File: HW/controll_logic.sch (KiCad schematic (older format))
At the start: 24 parts, among them J5 POWER_IN, J6 JTAG, J8 Stop System, SW1 RESET, U10 TL7705B, U11 ispMACH4A, U9 74HC74, X2 16MHz

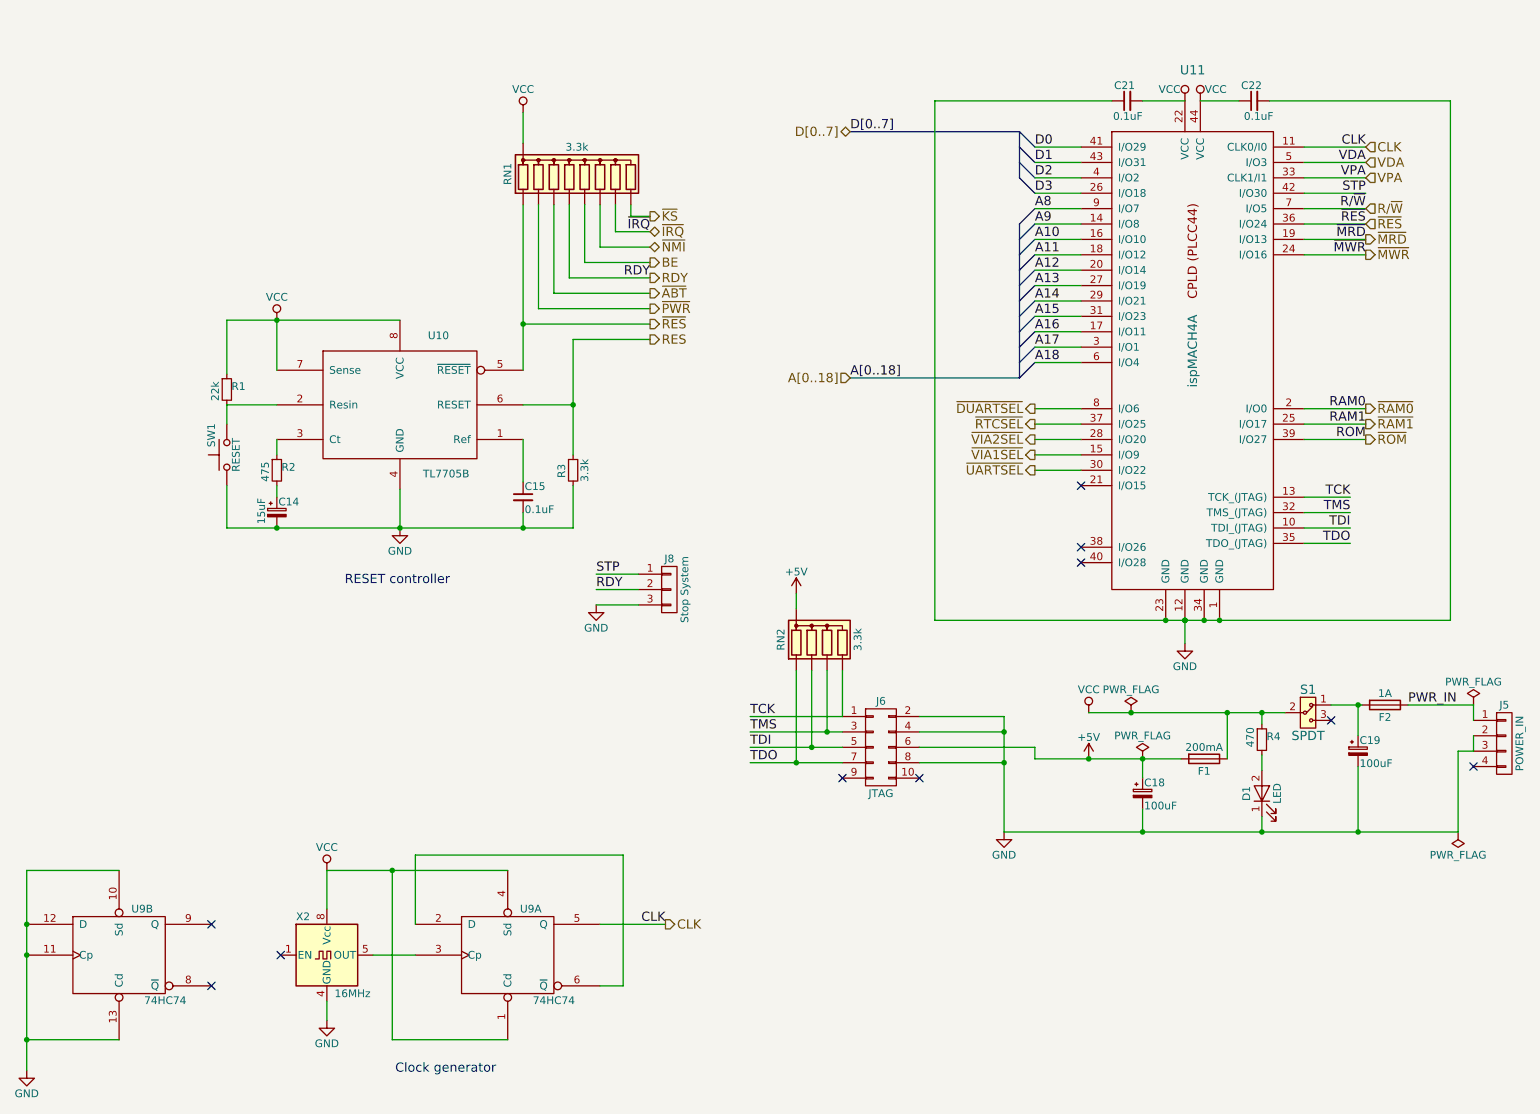
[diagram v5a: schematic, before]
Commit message: Added BDD CPLD code 0.5.1
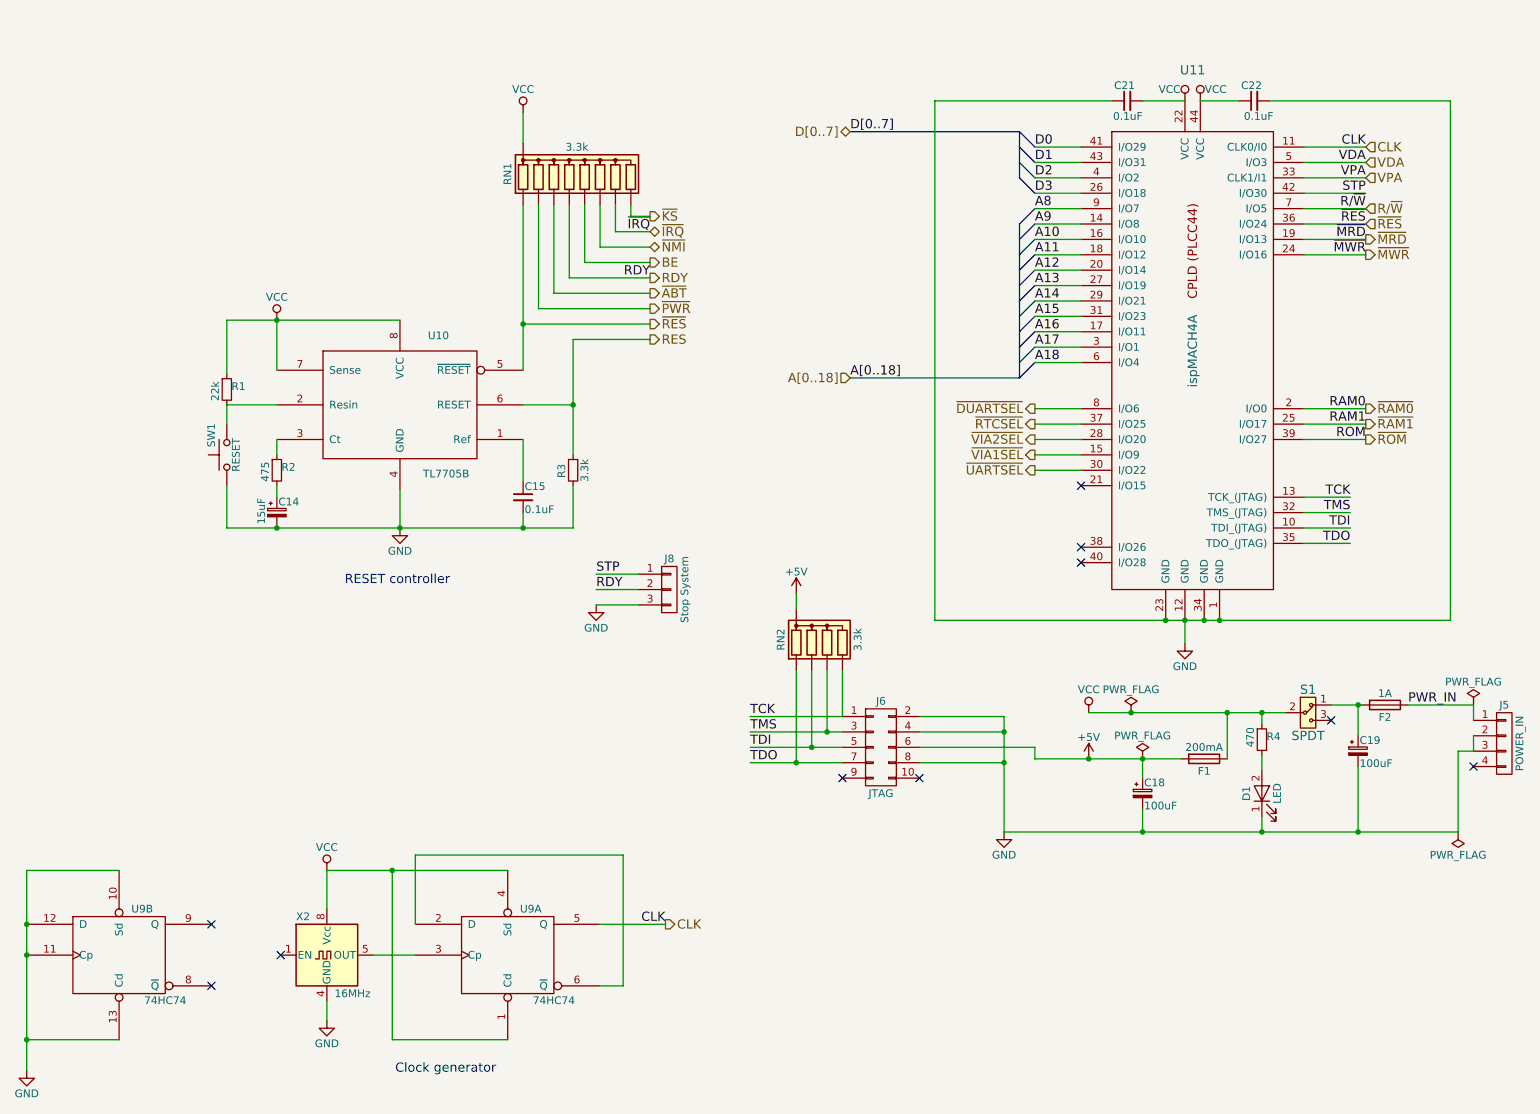
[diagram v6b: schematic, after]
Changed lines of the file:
@@
 	2650 6075 2650 6325
 Wire Wire Line
-	2650 6075 3075 6075
-Wire Wire Line
-	3075 6075 3825 6075
+	2650 6075 3825 6075
 Wire Wire Line
 	3825 7175 3075 7175
@@
 	1300 6075 700  6075
 Wire Wire Line
-	700  6075 700  6425
-Wire Wire Line
-	700  6425 700  6625
-Wire Wire Line
-	700  6625 700  7175
-Wire Wire Line
-	700  7175 700  7375
+	700  6075 700  7375
 Connection ~ 700  6425
 Connection ~ 700  6625
@@
 	4025 2425 4750 2425
 Wire Wire Line
-	3925 1750 3925 2525
-Wire Wire Line
-	3925 2525 3925 2825
+	3925 1750 3925 2825
 Wire Wire Line
 	3925 2525 4750 2525
@@
 	3925 3050 4250 3050
 Wire Wire Line
-	4250 2625 4250 3050
-Wire Wire Line
-	4250 3050 4250 3375
+	4250 2625 4250 3375
 Wire Wire Line
 	4250 2625 4750 2625
@@
 	2325 3575 2325 3650
 Wire Wire Line
-	2000 3850 2325 3850
-Wire Wire Line
-	2325 3850 3125 3850
-Wire Wire Line
-	3125 3850 3925 3850
-Wire Wire Line
-	3925 3850 4250 3850
+	2000 3850 4250 3850
 Wire Wire Line
 	3125 3850 3125 3600
 Wire Wire Line
-	2000 2500 2325 2500
-Wire Wire Line
-	2325 2500 3125 2500
+	2000 2500 3125 2500
 Wire Wire Line
 	2325 2500 2325 2825
@@
 	10100 5300 10000 5300
 Wire Wire Line
-	10000 5300 10000 5825
-Wire Wire Line
-	9175 5000 9350 5000
-Wire Wire Line
-	9350 5000 9375 5000
+	10000 5825 10000 5300
+Wire Wire Line
+	9175 5000 9375 5000
 Wire Wire Line
 	9350 5200 9350 5000
@@
 	9350 5400 9350 5825
 Wire Wire Line
-	10000 5825 9350 5825
-Wire Wire Line
-	9350 5825 8725 5825
-Wire Wire Line
-	8725 5825 7950 5825
-Wire Wire Line
-	7950 5825 7050 5825
+	7050 5825 10000 5825
 Wire Wire Line
 	8725 5725 8725 5825
@@
 Connection ~ 8725 5050
 Wire Wire Line
-	7250 5350 7600 5350
-Wire Wire Line
-	7600 5350 7950 5350
-Wire Wire Line
-	7950 5350 8200 5350
-Wire Wire Line
-	8500 5350 8500 5050
+	7250 5350 8200 5350
+Wire Wire Line
+	8500 5050 8500 5350
 Connection ~ 8500 5050
 Wire Wire Line
@@
 	6500 5075 7050 5075
 Wire Wire Line
-	7050 5075 7050 5175
-Wire Wire Line
-	7050 5175 7050 5375
-Wire Wire Line
-	7050 5375 7050 5825
+	7050 5075 7050 5825
 Wire Wire Line
 	6500 5375 7050 5375
@@
 	6000 5075 5400 5075
 Wire Wire Line
-	5400 5175 5900 5175
-Wire Wire Line
-	5900 5175 6000 5175
-Wire Wire Line
-	5400 5275 5800 5275
-Wire Wire Line
-	5800 5275 6000 5275
-Wire Wire Line
-	5400 5375 5700 5375
-Wire Wire Line
-	5700 5375 6000 5375
+	5400 5175 6000 5175
+Wire Wire Line
+	5400 5275 6000 5275
+Wire Wire Line
+	5400 5375 6000 5375
 Wire Wire Line
 	6000 5075 6000 4775
@@
 Connection ~ 7600 5350
 Wire Wire Line
-	7600 5050 7875 5050
-Wire Wire Line
-	7875 5050 8500 5050
-Wire Wire Line
-	8500 5050 8725 5050
-Wire Wire Line
-	8725 5050 8875 5050
+	7600 5050 8875 5050
 Wire Wire Line
 	6500 5175 7050 5175
@@
 	8225 1075 7950 1075
 Wire Wire Line
-	6600 4450 8100 4450
-Wire Wire Line
-	8100 4450 8225 4450
-Wire Wire Line
-	8225 4450 8225 4450
-Wire Wire Line
-	8225 4450 8350 4450
-Wire Wire Line
-	8350 4450 8450 4450
-Wire Wire Line
-	8450 4450 9950 4450
+	6600 4450 9950 4450
 Wire Wire Line
 	9950 4450 9950 1075
@@
 Wire Wire Line
 	8225 4600 8225 4450
-Connection ~ 8225 4450
 Wire Wire Line
 	9000 1375 9400 1375
@@
 	7550 2775 7250 2775
 Wire Bus Line
-	7150 1275 7150 1375
-Wire Bus Line
-	7150 1375 7150 1475
-Wire Bus Line
-	7150 1475 7150 1575
+	7150 1275 7150 1575
 Wire Bus Line
 	7150 1275 6050 1275
 Wire Bus Line
-	7150 1875 7150 1975
-Wire Bus Line
-	7150 1975 7150 2075
-Wire Bus Line
-	7150 2075 7150 2175
-Wire Bus Line
-	7150 2175 7150 2275
-Wire Bus Line
-	7150 2275 7150 2375
-Wire Bus Line
-	7150 2375 7150 2475
-Wire Bus Line
-	7150 2475 7150 2575
-Wire Bus Line
-	7150 2575 7150 2675
-Wire Bus Line
-	7150 2675 7150 2775
-Wire Bus Line
-	7150 2775 7150 2875
+	7150 1875 7150 2875
 Wire Bus Line
 	7150 2875 6050 2875

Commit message: Removed two ram chips, down to 1 MiB.
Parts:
- removed RN2: 3.3k, Resistors_THT:R_Array_SIP5, symbol R_Network04
- added H1, H2, H3, H4: MountingHole, Mounting_Holes:MountingHole_3.2mm_M3_DIN965_Pad, symbol Mechanical:MountingHole
- added JP1: Enable ISP, Pin_Headers:Pin_Header_Straight_1x02_Pitch2.54mm, symbol Device:Jumper_NO_Small
- added Q1: DS1813, TO_SOT_Packages_THT:TO-92_Inline_Narrow_Oval, symbol device:Q_NPN_EBC
- added RN2: 3.3k, Resistors_THT:R_Array_SIP5, symbol device:R_Network04
- added SW2: PANIC, Buttons_Switches_ThroughHole:SW_PUSH_6mm_h4.3mm, symbol switches:SW_Push
- C14, C18, C19: symbol CP_Small -> device:CP_Small
- C15, C21, C22: symbol C_Small -> device:C_Small
- D1: symbol LED -> device:LED
- F1, F2: symbol Fuse -> device:Fuse
- J5: symbol CONN_01X04 -> conn:CONN_01X04
- J6: symbol CONN_02X05 -> conn:CONN_02X05
- J8: symbol CONN_01X03 -> conn:CONN_01X03
- R1, R2, R3, R4: symbol R_Small -> device:R_Small
- RN1: symbol R_Network08 -> device:R_Network08
- S1: symbol SPDT -> saturn:SPDT
- SW1: symbol SW_Push -> switches:SW_Push
- U10: symbol TL7705B -> saturn:TL7705B
- U11: symbol ispMACH4A -> saturn:ispMACH4A
- U9: symbol 74HC74 -> 74xx1:74HC74
- X2: symbol CXO_DIP8 -> Oscillators:CXO_DIP8
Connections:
- net GND: now also Q1.3 (C), SW2.2
- net TCK: now also RN2.5 (R4)
- net TDI: now also RN2.3 (R2)
- net TDO: now also RN2.2 (R1)
- net TMS: now also RN2.4 (R3)
- net VCC: now also JP1.1, Q1.2 (B)
- net ~NMI: now also Q1.1 (E), SW2.1
- net ~RAM2: now reaches U11.21 (I/O15)
- net ~IOSEL3: now reaches U11.38 (I/O26)
- net ~IOSEL2: now reaches U11.40 (I/O28)
- net ~UARTSEL renamed ~RAM3
- new net: JP1.2, RN2.1 (common)
- no-connect marks 10 -> 7
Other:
- note added: "NMI Debouncer"
- moved on the sheet: J6, J8
